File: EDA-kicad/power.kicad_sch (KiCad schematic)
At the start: 93 parts, among them SW1 EG25-switch-CSS-1210MC, SW2 MIC-switch-CSS-1210MC, SW3 CAM-switch-CSS-1210MC, U11 TPS65023BRSBR, U4 BQ25792RQMR, U6 BAT-CONNECTOR-FLTS22WR00, U7 22V-boost-AP3032KTR-G1, U8 MP3429GL-Z

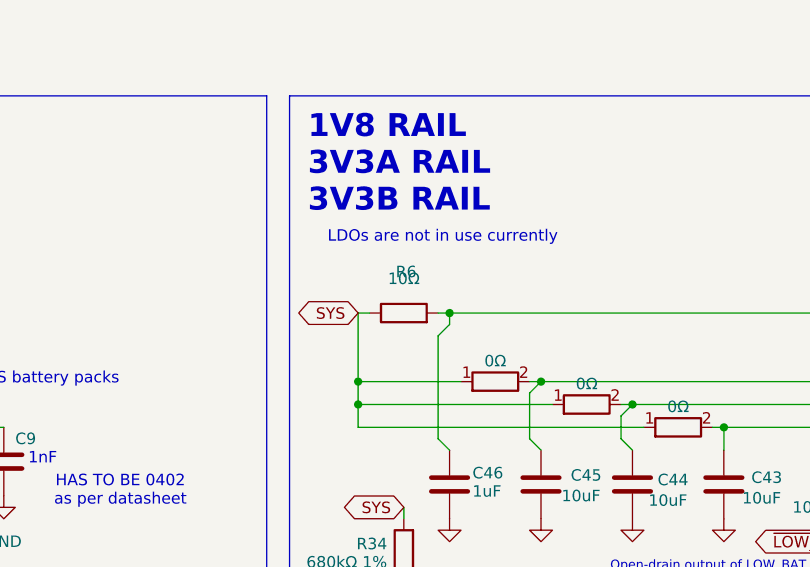
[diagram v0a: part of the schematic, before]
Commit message: Fixed audio schematic file name
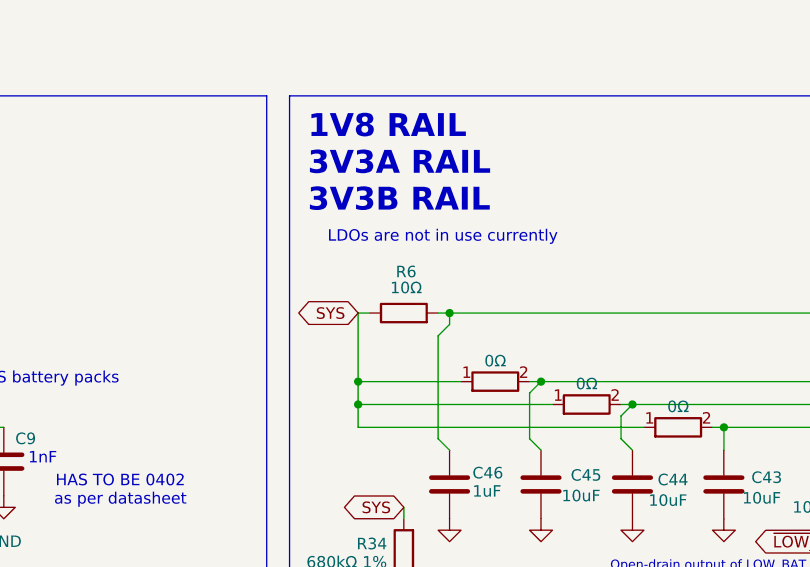
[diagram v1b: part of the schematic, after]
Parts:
- added R18: 10kΩ, SPIRIT-footprints:0603-resistor, symbol Device:R
- added R39: 10k, SPIRIT-footprints:0603-resistor, symbol Device:R
- R38: renamed from R18; value 10kΩ -> 10k
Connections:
- net 3V3B: now also R39.2; no longer R38.2
- net SCL PMIC: now also R39.1; no longer R38.1
- net VCC: now also R18.1; no longer R38.1
- net ~{BQ INT}: now also R18.2; no longer R38.2
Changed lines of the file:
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@@
 		)
 		(property "Value" "10Ω"
-			(at 248.92 71.12 90)
+			(at 249.174 72.136 90)
 			(effects
 				(font

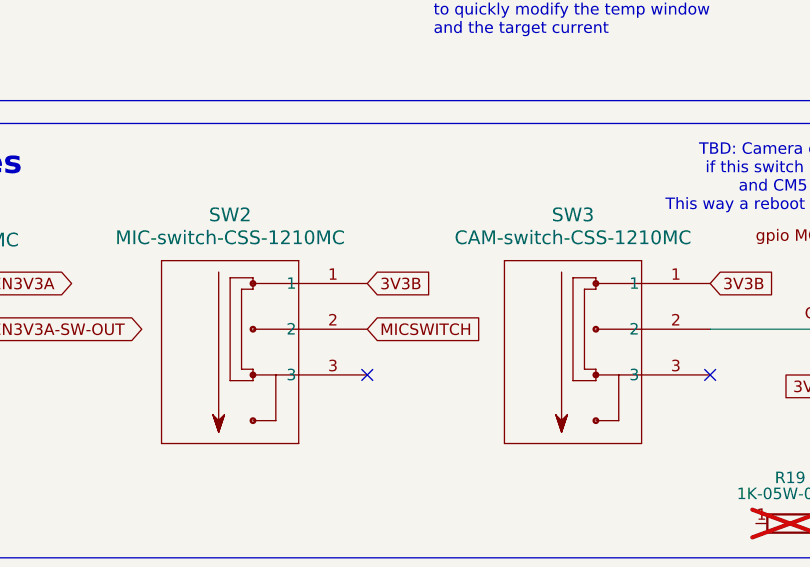
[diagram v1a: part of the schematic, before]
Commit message: change netflaf for microphone switch to be 1V8 instead of 3V3B, GPS/GSM symbol
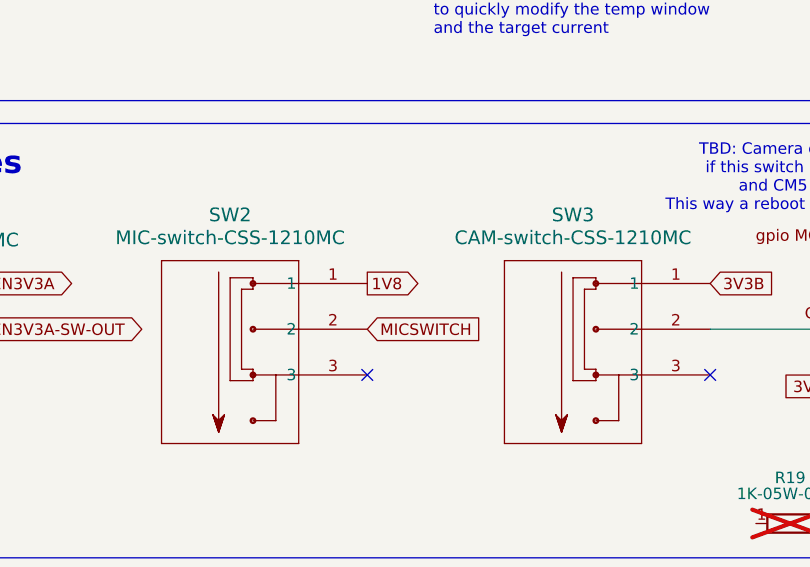
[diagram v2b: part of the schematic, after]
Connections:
- net 1V8: now also SW2.1
- net 3V3B: no longer SW2.1
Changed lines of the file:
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@@
 		)
 	)
-	(global_label "3V3B"
-		(shape input)
+	(global_label "1V8"
+		(shape output)
 		(at 153.67 180.34 0)
 		(fields_autoplaced yes)

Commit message: reannotate entire schematic
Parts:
- renumbered C7 to C29, C8 to C30, C9 to C31, C46 to C32, C45 to C33, C44 to C34, C43 to C35, C25 to C36, C10 to C37, C11 to C38, C12 to C39, C13 to C40, C14 to C41, C15 to C42, C24 to C43, C16 to C44, C17 to C45, C18 to C46, C19 to C47, C20 to C48, C21 to C49, C22 to C50, C47 to C51, C23 to C52, C30 to C53, C31 to C54, C32 to C55, C33 to C56, C34 to C57, C35 to C58, C36 to C59, C37 to C60, C38 to C61, C39 to C62, C40 to C63, C41 to C64, C42 to C65, L9 to L1, L8 to L2, L1 to L3, L7 to L4, R5 to R10, R6 to R11, R7 to R12, R9 to R13, R12 to R14, R35 to R15, R36 to R16, R11 to R17, R29 to R18, R34 to R19, R10 to R20, R8 to R21, R32 to R22, R37 to R23, R13 to R24, R14 to R25, R33 to R26, R15 to R27, R16 to R28, R17 to R29, R18 to R30, R28 to R32, R30 to R33, R26 to R34, R27 to R35, R19 to R36, R20 to R37, R21 to R38, R22 to R39, R23 to R40, R4 to R7, R39 to R8, R38 to R9, TP7 to TP3, TP6 to TP4, TP8 to TP6, U7 to U10, U8 to U11, U4 to U7, U11 to U8, U6 to U9

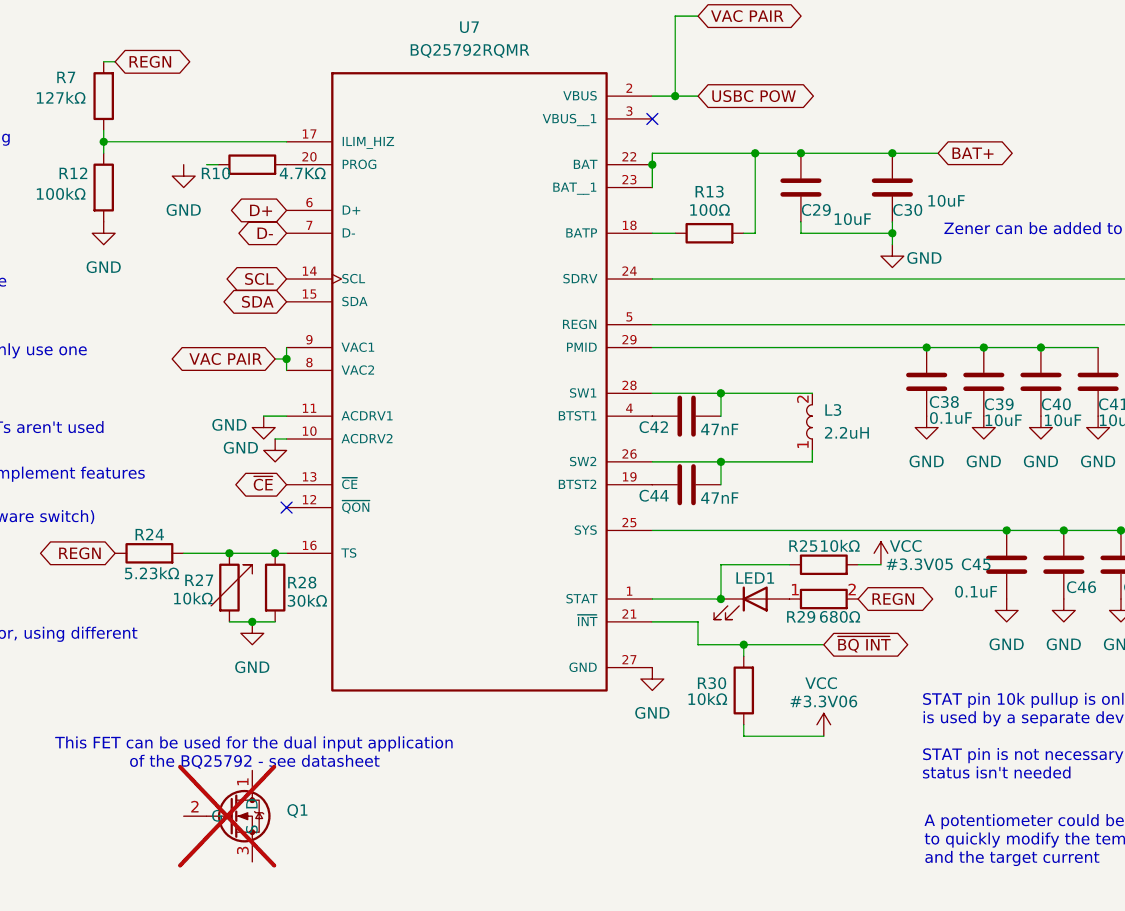
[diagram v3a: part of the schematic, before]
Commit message: broken connection, change flags to 3V3B labels
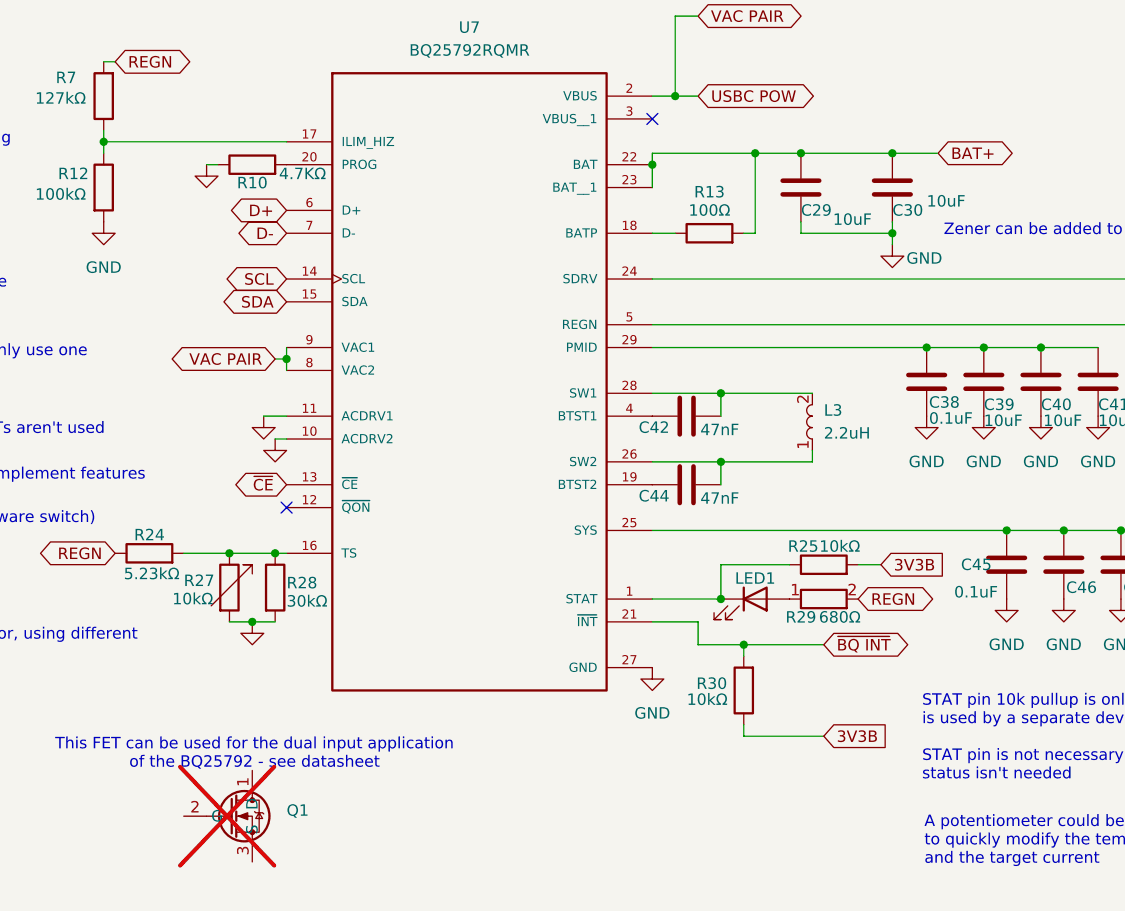
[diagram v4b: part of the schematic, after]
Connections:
- net VCC is gone; now on net 3V3B: R25.2, R30.1
- net GND: now also R10.1
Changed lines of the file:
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@@
 		)
 	)
+	(global_label "3V3B"
+		(shape input)
+		(at 149.86 138.43 0)
+		(fields_autoplaced yes)
+		(effects
+			(font
+				(size 1.27 1.27)
+			)
+			(justify left)
+		)
+		(property "Intersheetrefs" "${INTERSHEET_REFS}"
+			(at 157.6228 138.43 0)
+			(effects
+				(font
+					(size 1.27 1.27)
+				)
+				(justify left)
+				(hide yes)
+			)
+		)
+	)
 	(global_label "LCD_PWM"
 		(shape bidirectional)
@@
 		)
 	)
+	(global_label "3V3B"
+		(shape input)
+		(at 156.21 119.38 0)
+		(fields_autoplaced yes)
+		(effects
+			(font
+				(size 1.27 1.27)
+			)
+			(justify left)
+		)
+		(property "Intersheetrefs" "${INTERSHEET_REFS}"
+			(at 163.9728 119.38 0)
+			(effects
+				(font
+					(size 1.27 1.27)
+				)
+				(justify left)
+				(hide yes)
+			)
+		)
+	)
 	(global_label "DEFDCDC1 DIVIDER"
 		(shape input)
@@
 		(dnp no)
 		(property "Reference" "R10"
-			(at 82.296 75.946 90)
+			(at 86.36 76.962 90)
 			(effects
 				(font
@@
 		(lib_name "GND_1")
 		(lib_id "power:GND")
-		(at 78.74 74.93 0)
+		(at 81.28 74.93 0)
 		(unit 1)
 		(exclude_from_sim no)
@@
 		(fields_autoplaced yes)
 		(property "Reference" "#PWR086"
-			(at 78.74 81.28 0)
+			(at 81.28 81.28 0)
 			(effects
 				(font
@@
 		)
 		(property "Value" "GND"
-			(at 78.74 80.01 0)
+			(at 81.28 80.01 0)
 			(effects
 				(font
 					(size 1.27 1.27)
 				)
+				(hide yes)
 			)
 		)
 		(property "Footprint" ""
-			(at 78.74 74.93 0)
+			(at 81.28 74.93 0)
 			(effects
 				(font
@@
 		)
 		(property "Datasheet" ""
-			(at 78.74 74.93 0)
+			(at 81.28 74.93 0)
 			(effects
 				(font
@@
 		)
 		(property "Description" "Power symbol creates a global label with name \"GND\" , ground"
-			(at 78.74 74.93 0)
+			(at 81.28 74.93 0)
 			(effects
 				(font
@@
 					(size 1.27 1.27)
 				)
+				(hide yes)
 			)
 		)
@@
 					(size 1.27 1.27)
 				)
+				(hide yes)
 			)
 		)
@@
 	)
 	(symbol
-		(lib_name "VCC_1")
-		(lib_id "power:VCC")
-		(at 156.21 119.38 0)
-		(unit 1)
-		(exclude_from_sim no)
-		(in_bom yes)
-		(on_board yes)
-		(dnp no)
-		(property "Reference" "#3.3V05"
-			(at 160.528 119.38 0)
-			(effects
-				(font
-					(size 1.27 1.27)
-				)
-			)
-		)
-		(property "Value" "VCC"
-			(at 159.004 117.348 0)
-			(effects
-				(font
-					(size 1.27 1.27)
-				)
-			)
-		)
-		(property "Footprint" ""
-			(at 156.21 119.38 0)
-			(effects
-				(font
-					(size 1.27 1.27)
-				)
-				(hide yes)
-			)
-		)
-		(property "Datasheet" ""
-			(at 156.21 119.38 0)
-			(effects
-				(font
-					(size 1.27 1.27)
-				)
-				(hide yes)
-			)
-		)
-		(property "Description" ""
-			(at 156.21 119.38 0)
-			(effects
-				(font
-					(size 1.27 1.27)
-				)
-				(hide yes)
-			)
-		)
-		(pin "1"
-		)
-		(instances
-			(project "cm5-carrier"
-				(path "/28c5e4fe-1ec7-4477-97f0-d2ec1401fad5/59851108-1ec5-49a1-aa9b-d5428f895885"
-					(reference "#3.3V05")
-					(unit 1)
-				)
-			)
-			(project "power"
-				(path "/446f2954-4486-4a73-ab5d-988e1515679d"
-					(reference "#3.3V?")
-					(unit 1)
-				)
-			)
-		)
-	)
-	(symbol
 		(lib_name "GND_6")
 		(lib_id "power:GND")
@@
 	)
 	(symbol
-		(lib_id "power:VCC")
-		(at 149.86 138.43 0)
-		(unit 1)
-		(exclude_from_sim no)
-		(in_bom yes)
-		(on_board yes)
-		(dnp no)
-		(property "Reference" "#3.3V06"
-			(at 149.86 134.62 0)
-			(effects
-				(font
-					(size 1.27 1.27)
-				)
-			)
-		)
-		(property "Value" "VCC"
-			(at 149.606 132.588 0)
-			(effects
-				(font
-					(size 1.27 1.27)
-				)
-			)
-		)
-		(property "Footprint" ""
-			(at 149.86 138.43 0)
-			(effects
-				(font
-					(size 1.27 1.27)
-				)
-				(hide yes)
-			)
-		)
-		(property "Datasheet" ""
-			(at 149.86 138.43 0)
-			(effects
-				(font
-					(size 1.27 1.27)
-				)
-				(hide yes)
-			)
-		)
-		(property "Description" ""
-			(at 149.86 138.43 0)
-			(effects
-				(font
-					(size 1.27 1.27)
-				)
-				(hide yes)
-			)
-		)
-		(pin "1"
-		)
-		(instances
-			(project "cm5-carrier"
-				(path "/28c5e4fe-1ec7-4477-97f0-d2ec1401fad5/59851108-1ec5-49a1-aa9b-d5428f895885"
-					(reference "#3.3V06")
-					(unit 1)
-				)
-			)
-			(project "power"
-				(path "/446f2954-4486-4a73-ab5d-988e1515679d"
-					(reference "#3.3V?")
-					(unit 1)
-				)
-			)
-		)
-	)
-	(symbol
 		(lib_name "GND_4")
 		(lib_id "power:GND")
@@
 					(size 1.27 1.27)
 				)
+				(hide yes)
 			)
 		)

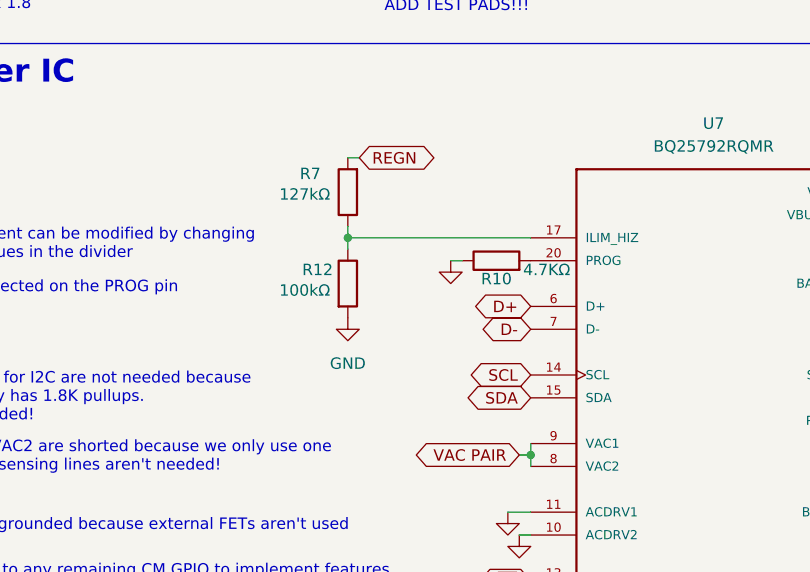
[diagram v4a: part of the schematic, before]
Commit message: charger 50% routed
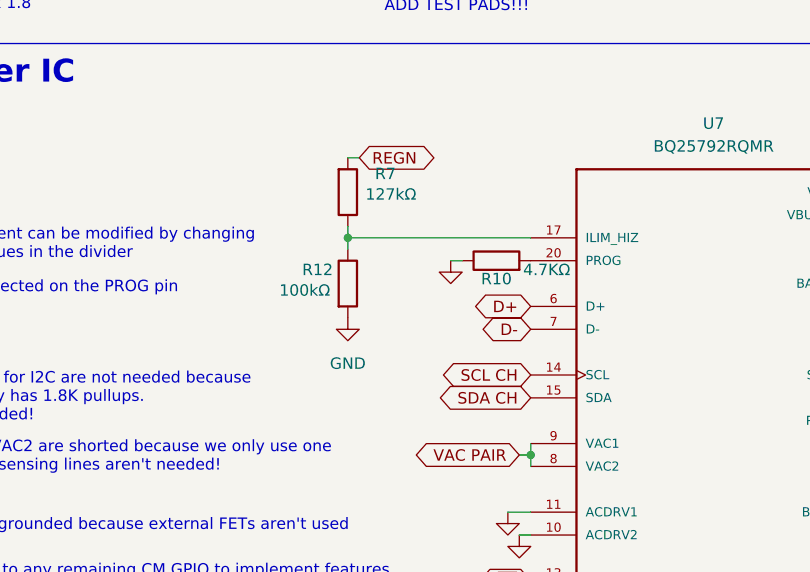
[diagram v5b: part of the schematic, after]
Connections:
- net SCL renamed SCL CH
- net SDA renamed SDA CH
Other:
- moved on the sheet: R7
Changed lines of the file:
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@@
 		)
 	)
-	(global_label "SDA"
+	(global_label "SDA CH"
 		(shape bidirectional)
 		(at 90.17 90.17 180)
@@
 		)
 		(property "Intersheetrefs" "${INTERSHEET_REFS}"
-			(at 82.5054 90.17 0)
+			(at 78.9373 90.17 0)
 			(effects
 				(font
@@
 		)
 	)
-	(global_label "SCL"
+	(global_label "SCL CH"
 		(shape bidirectional)
 		(at 90.17 87.63 180)
@@
 		)
 		(property "Intersheetrefs" "${INTERSHEET_REFS}"
-			(at 82.5659 87.63 0)
+			(at 78.9978 87.63 0)
 			(effects
 				(font
@@
 		(on_board yes)
 		(dnp no)
-		(fields_autoplaced yes)
 		(property "Reference" "U7"
 			(at 110.49 59.69 0)
@@
 	(symbol
 		(lib_id "Device:R")
-		(at 69.85 67.31 180)
+		(at 69.85 67.31 0)
+		(mirror x)
 		(unit 1)
 		(exclude_from_sim no)
@@
 		(dnp no)
 		(property "Reference" "R7"
-			(at 64.516 65.278 0)
+			(at 75.184 65.278 0)
 			(effects
 				(font
@@
 		)
 		(property "Value" "127kΩ"
-			(at 62.23 67.564 0)
+			(at 77.47 67.564 0)
 			(effects
 				(font
@@
 		)
 		(property "Footprint" "SPIRIT-footprints:0805-resistor"
-			(at 71.628 67.31 90)
+			(at 68.072 67.31 90)
 			(effects
 				(font

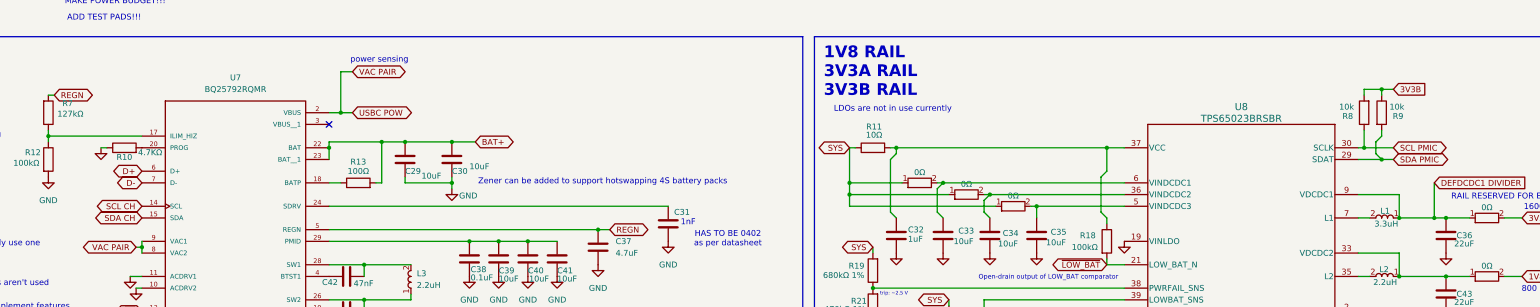
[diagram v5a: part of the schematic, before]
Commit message: remove redundant pull ups, connect charger and PMIC on single I2C bus
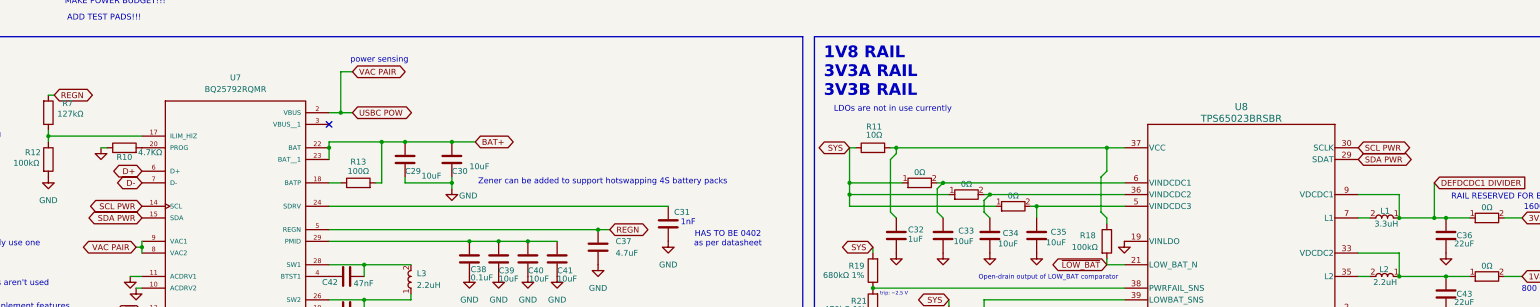
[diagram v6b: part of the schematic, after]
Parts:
- removed R8, R9: 10k, SPIRIT-footprints:0603-resistor, symbol Device:R
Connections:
- net SCL PMIC is gone; now on net SCL PWR: U8.30 (SCLK)
- net SDA PMIC is gone; now on net SDA PWR: U8.29 (SDAT)
- net SCL CH renamed SCL PWR
- net SDA CH renamed SDA PWR

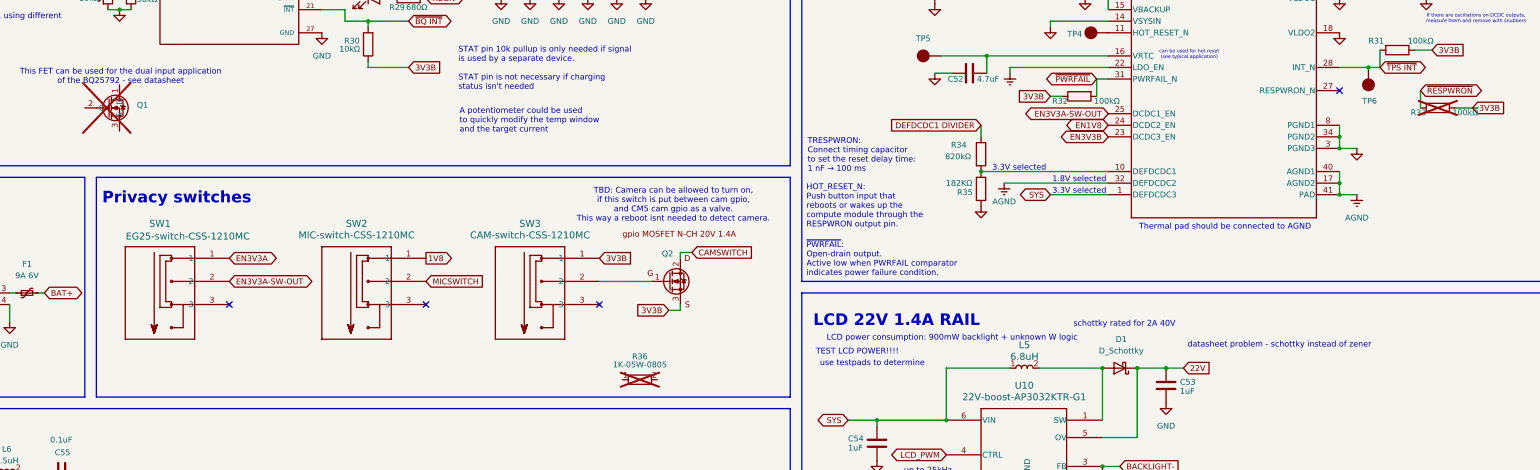
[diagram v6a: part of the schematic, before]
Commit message: connect USB switch
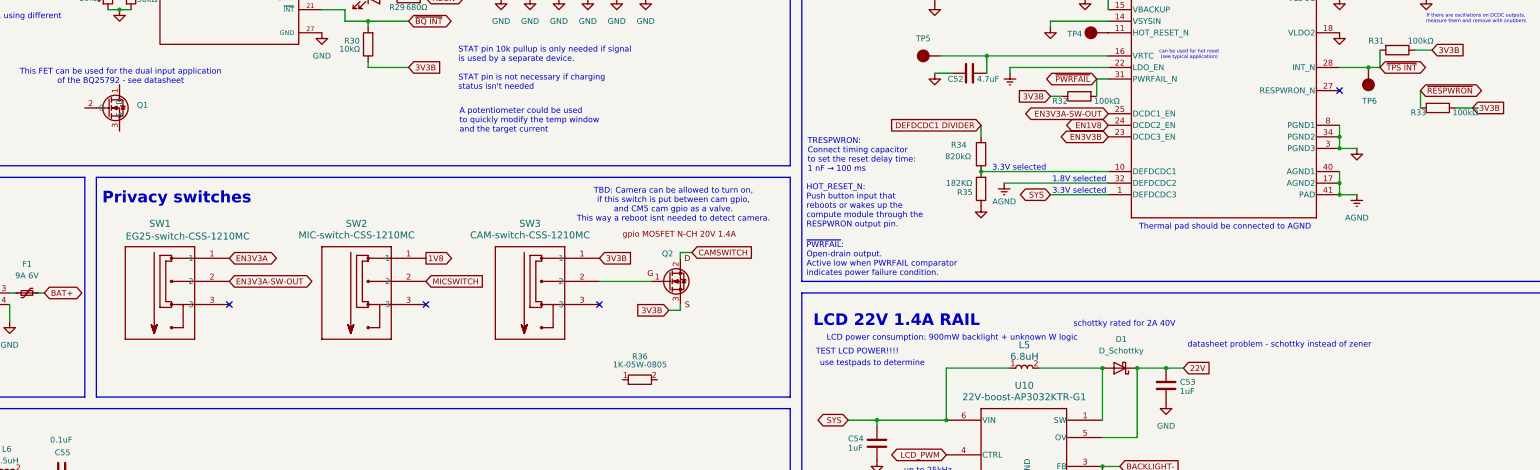
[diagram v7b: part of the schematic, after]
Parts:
- Q1, R33, R36: now fitted
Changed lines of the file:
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@@
 		(in_bom no)
 		(on_board no)
-		(dnp yes)
+		(dnp no)
 		(property "Reference" "R36"
 			(at 200.66 201.93 0)
@@
 		(in_bom yes)
 		(on_board yes)
-		(dnp yes)
+		(dnp no)
 		(fields_autoplaced yes)
 		(property "Reference" "Q1"
@@
 		(in_bom yes)
 		(on_board yes)
-		(dnp yes)
+		(dnp no)
 		(property "Reference" "R33"
 			(at 373.38 148.336 90)
